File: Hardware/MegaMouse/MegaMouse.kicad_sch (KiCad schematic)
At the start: 0 parts

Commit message: Brake lights!
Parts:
- added BT101: Battery_Cell, Battery:BatteryHolder_MPD_BH-18650-PC2, symbol Device:Battery_Cell
- added D101, D102: BrakeLight, LED_THT:LED_D3.0mm_Horizontal_O1.27mm_Z2.0mm, symbol Device:LED
- added D103: TurnL, LED_THT:LED_D3.0mm_Horizontal_O6.35mm_Z6.0mm, symbol Device:LED
- added D104: TurnR, LED_THT:LED_D3.0mm_Horizontal_O6.35mm_Z6.0mm, symbol Device:LED
- added J101: MotorL, MegaMouse:MicroMotor, symbol Connector:Conn_01x05_Female
- added J102: MotorR, MegaMouse:MicroMotor, symbol Connector:Conn_01x05_Female
- added U101: ATmega328P-A, Package_QFP:TQFP-32_7x7mm_P0.8mm, symbol MCU_Microchip_ATmega:ATmega328P-A
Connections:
- new net: U101.21 (GND), U101.3 (GND), U101.5 (GND)
- new net: U101.4 (VCC), U101.6 (VCC)
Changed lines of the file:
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@@
 (kicad_sch (version 20211123) (generator eeschema)
   (paper "A4")
+  (symbol (lib_id "Device:LED") (at 71.755 76.835 180) (unit 1)
+    (in_bom yes) (on_board yes) (fields_autoplaced)
+    (property "Reference" "D101" (id 0) (at 73.3425 69.85 0))
+    (property "Value" "BrakeLight" (id 1) (at 73.3425 72.39 0))
+    (property "Footprint" "LED_THT:LED_D3.0mm_Horizontal_O1.27mm_Z2.0mm" (id 2) (at 71.755 76.835 0)
+      (effects (font (size 1.27 1.27)) hide)
+    )
+    (property "Datasheet" "~" (id 3) (at 71.755 76.835 0)
+      (effects (font (size 1.27 1.27)) hide)
+    )
+    (pin "1")
+    (pin "2")
+  )
+  (symbol (lib_id "Device:Battery_Cell") (at 234.95 49.53 0) (unit 1)
+    (in_bom yes) (on_board yes) (fields_autoplaced)
+    (property "Reference" "BT101" (id 0) (at 238.76 46.2279 0)
+      (effects (font (size 1.27 1.27)) (justify left))
+    )
+    (property "Value" "Battery_Cell" (id 1) (at 238.76 48.7679 0)
+      (effects (font (size 1.27 1.27)) (justify left))
+    )
+    (property "Footprint" "Battery:BatteryHolder_MPD_BH-18650-PC2" (id 2) (at 234.95 48.006 90)
+      (effects (font (size 1.27 1.27)) hide)
+    )
+    (property "Datasheet" "~" (id 3) (at 234.95 48.006 90)
+      (effects (font (size 1.27 1.27)) hide)
+    )
+    (pin "1")
+    (pin "2")
+  )
+  (symbol (lib_id "MCU_Microchip_ATmega:ATmega328P-A") (at 142.24 96.52 0) (unit 1)
+    (in_bom yes) (on_board yes) (fields_autoplaced)
+    (property "Reference" "U101" (id 0) (at 144.2594 134.62 0)
+      (effects (font (size 1.27 1.27)) (justify left))
+    )
+    (property "Value" "ATmega328P-A" (id 1) (at 144.2594 137.16 0)
+      (effects (font (size 1.27 1.27)) (justify left))
+    )
+    (property "Footprint" "Package_QFP:TQFP-32_7x7mm_P0.8mm" (id 2) (at 142.24 96.52 0)
+      (effects (font (size 1.27 1.27) italic) hide)
+    )
+    (property "Datasheet" "http://ww1.microchip.com/downloads/en/DeviceDoc/ATmega328_P%20AVR%20MCU%20with%20picoPower%20Technology%20Data%20Sheet%2040001984A.pdf" (id 3) (at 142.24 96.52 0)
+      (effects (font (size 1.27 1.27)) hide)
+    )
+    (pin "1")
+    (pin "10")
+    (pin "11")
+    (pin "12")
+    (pin "13")
+    (pin "14")
+    (pin "15")
+    (pin "16")
+    (pin "17")
+    (pin "18")
+    (pin "19")
+    (pin "2")
+    (pin "20")
+    (pin "21")
+    (pin "22")
+    (pin "23")
+    (pin "24")
+    (pin "25")
+    (pin "26")
+    (pin "27")
+    (pin "28")
+    (pin "29")
+    (pin "3")
+    (pin "30")
+    (pin "31")
+    (pin "32")
+    (pin "4")
+    (pin "5")
+    (pin "6")
+    (pin "7")
+    (pin "8")
+    (pin "9")
+  )
+  (symbol (lib_id "Device:LED") (at 85.09 76.835 180) (unit 1)
+    (in_bom yes) (on_board yes) (fields_autoplaced)
+    (property "Reference" "D103" (id 0) (at 86.6775 69.215 0))
+    (property "Value" "TurnL" (id 1) (at 86.6775 71.755 0))
+    (property "Footprint" "LED_THT:LED_D3.0mm_Horizontal_O6.35mm_Z6.0mm" (id 2) (at 85.09 76.835 0)
+      (effects (font (size 1.27 1.27)) hide)
+    )
+    (property "Datasheet" "~" (id 3) (at 85.09 76.835 0)
+      (effects (font (size 1.27 1.27)) hide)
+    )
+    (pin "1")
+    (pin "2")
+  )
+  (symbol (lib_id "Device:LED") (at 85.09 87.63 180) (unit 1)
+    (in_bom yes) (on_board yes) (fields_autoplaced)
+    (property "Reference" "D104" (id 0) (at 86.6775 80.01 0))
+    (property "Value" "TurnR" (id 1) (at 86.6775 82.55 0))
+    (property "Footprint" "LED_THT:LED_D3.0mm_Horizontal_O6.35mm_Z6.0mm" (id 2) (at 85.09 87.63 0)
+      (effects (font (size 1.27 1.27)) hide)
+    )
+    (property "Datasheet" "~" (id 3) (at 85.09 87.63 0)
+      (effects (font (size 1.27 1.27)) hide)
+    )
+    (pin "1")
+    (pin "2")
+  )
+  (symbol (lib_id "Device:LED") (at 71.755 87.63 180) (unit 1)
+    (in_bom yes) (on_board yes) (fields_autoplaced)
+    (property "Reference" "D102" (id 0) (at 73.3425 80.645 0))
+    (property "Value" "BrakeLight" (id 1) (at 73.3425 83.185 0))
+    (property "Footprint" "LED_THT:LED_D3.0mm_Horizontal_O1.27mm_Z2.0mm" (id 2) (at 71.755 87.63 0)
+      (effects (font (size 1.27 1.27)) hide)
+    )
+    (property "Datasheet" "~" (id 3) (at 71.755 87.63 0)
+      (effects (font (size 1.27 1.27)) hide)
+    )
+    (pin "1")
+    (pin "2")
+  )
+  (symbol (lib_id "Connector:Conn_01x05_Female") (at 205.74 85.725 0) (unit 1)
+    (in_bom yes) (on_board yes) (fields_autoplaced)
+    (property "Reference" "J101" (id 0) (at 207.01 84.4549 0)
+      (effects (font (size 1.27 1.27)) (justify left))
+    )
+    (property "Value" "MotorL" (id 1) (at 207.01 86.9949 0)
+      (effects (font (size 1.27 1.27)) (justify left))
+    )
+    (property "Footprint" "MegaMouse:MicroMotor" (id 2) (at 205.74 85.725 0)
+      (effects (font (size 1.27 1.27)) hide)
+    )
+    (property "Datasheet" "~" (id 3) (at 205.74 85.725 0)
+      (effects (font (size 1.27 1.27)) hide)
+    )
+    (pin "1")
+    (pin "2")
+    (pin "3")
+    (pin "4")
+    (pin "5")
+  )
+  (symbol (lib_id "Connector:Conn_01x05_Female") (at 222.25 85.725 0) (unit 1)
+    (in_bom yes) (on_board yes) (fields_autoplaced)
+    (property "Reference" "J102" (id 0) (at 223.52 84.4549 0)
+      (effects (font (size 1.27 1.27)) (justify left))
+    )
+    (property "Value" "MotorR" (id 1) (at 223.52 86.9949 0)
+      (effects (font (size 1.27 1.27)) (justify left))
+    )
+    (property "Footprint" "MegaMouse:MicroMotor" (id 2) (at 222.25 85.725 0)
+      (effects (font (size 1.27 1.27)) hide)
+    )
+    (property "Datasheet" "~" (id 3) (at 222.25 85.725 0)
+      (effects (font (size 1.27 1.27)) hide)
+    )
+    (pin "1")
+    (pin "2")
+    (pin "3")
+    (pin "4")
+    (pin "5")
+  )
   (sheet_instances
     (path "/" (page "1"))
   )
+  (symbol_instances
+    (path "/3108476a-847a-4adf-becb-69126938c9dd"
+      (reference "BT101") (unit 1) (value "Battery_Cell") (footprint "Battery:BatteryHolder_MPD_BH-18650-PC2")
+    )
+    (path "/0b0f8615-a521-40dd-95b3-c6dc98e26914"
+      (reference "D101") (unit 1) (value "BrakeLight") (footprint "LED_THT:LED_D3.0mm_Horizontal_O1.27mm_Z2.0mm")
+    )
+    (path "/b6bd84fa-c83d-44d0-90d2-a9564b93df9c"
+      (reference "D102") (unit 1) (value "BrakeLight") (footprint "LED_THT:LED_D3.0mm_Horizontal_O1.27mm_Z2.0mm")
+    )
+    (path "/87589939-cb7a-482a-9d88-508640d671a3"
+      (reference "D103") (unit 1) (value "TurnL") (footprint "LED_THT:LED_D3.0mm_Horizontal_O6.35mm_Z6.0mm")
+    )
+    (path "/b06c9f42-4c7e-4451-b623-83e43d24c5fc"
+      (reference "D104") (unit 1) (value "TurnR") (footprint "LED_THT:LED_D3.0mm_Horizontal_O6.35mm_Z6.0mm")
+    )
+    (path "/bd1226fe-f6ac-4ec8-9650-08c99a4f03a9"
+      (reference "J101") (unit 1) (value "MotorL") (footprint "MegaMouse:MicroMotor")
+    )
+    (path "/e73cdaaa-7743-4e85-b32f-0823784545c7"
+      (reference "J102") (unit 1) (value "MotorR") (footprint "MegaMouse:MicroMotor")
+    )
+    (path "/6237422b-5d80-4047-94aa-94384be9ec54"
+      (reference "U101") (unit 1) (value "ATmega328P-A") (footprint "Package_QFP:TQFP-32_7x7mm_P0.8mm")
+    )
+  )
 )

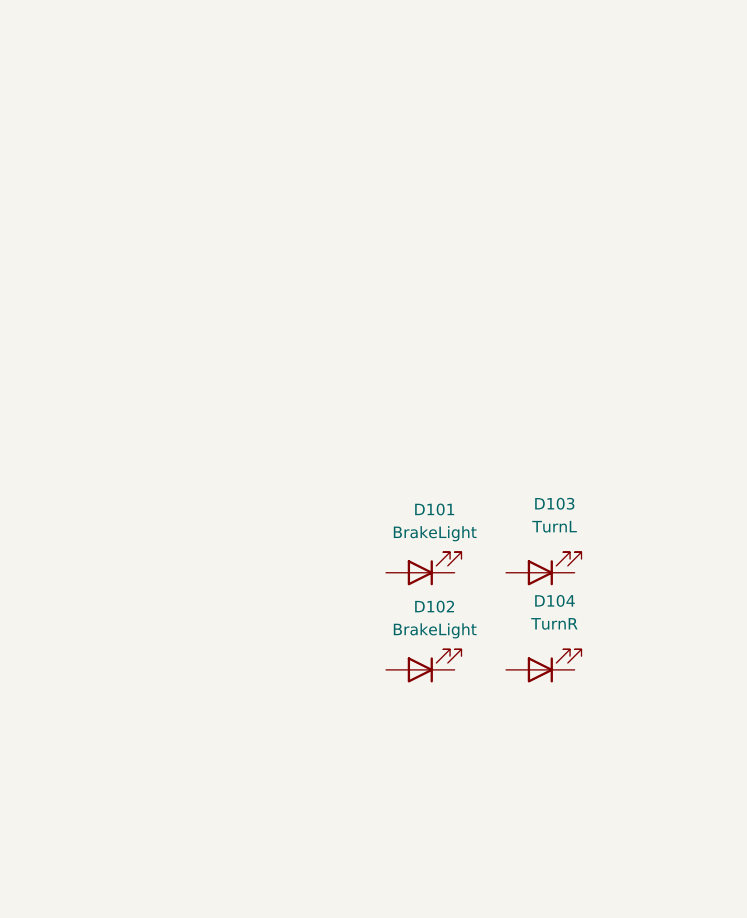
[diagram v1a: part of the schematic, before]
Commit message: Add brakelight as full kicad_mod
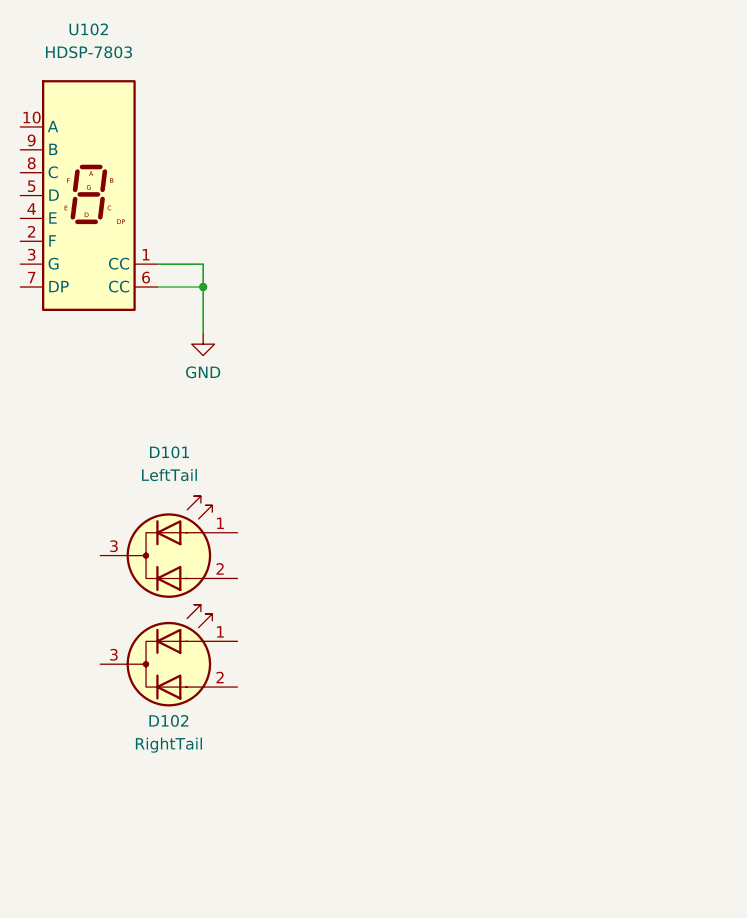
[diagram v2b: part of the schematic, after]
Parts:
- removed D101, D102: BrakeLight, LED_THT:LED_D3.0mm_Horizontal_O1.27mm_Z2.0mm, symbol Device:LED
- removed D103: TurnL, LED_THT:LED_D3.0mm_Horizontal_O6.35mm_Z6.0mm, symbol Device:LED
- removed D104: TurnR, LED_THT:LED_D3.0mm_Horizontal_O6.35mm_Z6.0mm, symbol Device:LED
- added D101: LeftTail, MegaMouse:BrakeLight, symbol Device:LED_Dual_AAK
- added D102: RightTail, MegaMouse:BrakeLight, symbol Device:LED_Dual_AAK
- added U102: HDSP-7803, Display_7Segment:HDSP-7801, symbol Display_Character:HDSP-7803
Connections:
- new net GND: U102.1 (CC), U102.6 (CC)
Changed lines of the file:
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@@
 (kicad_sch (version 20211123) (generator eeschema)
   (paper "A4")
-  (symbol (lib_id "Device:LED") (at 71.755 76.835 180) (unit 1)
-    (in_bom yes) (on_board yes) (fields_autoplaced)
-    (property "Reference" "D101" (id 0) (at 73.3425 69.85 0))
-    (property "Value" "BrakeLight" (id 1) (at 73.3425 72.39 0))
-    (property "Footprint" "LED_THT:LED_D3.0mm_Horizontal_O1.27mm_Z2.0mm" (id 2) (at 71.755 76.835 0)
-      (effects (font (size 1.27 1.27)) hide)
-    )
-    (property "Datasheet" "~" (id 3) (at 71.755 76.835 0)
-      (effects (font (size 1.27 1.27)) hide)
-    )
-    (pin "1")
-    (pin "2")
+  (junction (at 47.625 45.085) (diameter 0) (color 0 0 0 0)
+  )
+  (wire (pts (xy 47.625 42.545) (xy 47.625 45.085))
+    (stroke (width 0) (type default) (color 0 0 0 0))
+  )
+  (wire (pts (xy 42.545 42.545) (xy 47.625 42.545))
+    (stroke (width 0) (type default) (color 0 0 0 0))
+  )
+  (wire (pts (xy 47.625 45.085) (xy 47.625 50.165))
+    (stroke (width 0) (type default) (color 0 0 0 0))
+  )
+  (wire (pts (xy 42.545 45.085) (xy 47.625 45.085))
+    (stroke (width 0) (type default) (color 0 0 0 0))
+  )
+  (symbol (lib_id "Display_Character:HDSP-7803") (at 34.925 34.925 0) (unit 1)
+    (in_bom yes) (on_board yes) (fields_autoplaced)
+    (property "Reference" "U102" (id 0) (at 34.925 16.51 0))
+    (property "Value" "HDSP-7803" (id 1) (at 34.925 19.05 0))
+    (property "Footprint" "Display_7Segment:HDSP-7801" (id 2) (at 34.925 48.895 0)
+      (effects (font (size 1.27 1.27)) hide)
+    )
+    (property "Datasheet" "https://docs.broadcom.com/docs/AV02-2553EN" (id 3) (at 34.925 34.925 0)
+      (effects (font (size 1.27 1.27)) hide)
+    )
+    (pin "1")
+    (pin "10")
+    (pin "2")
+    (pin "3")
+    (pin "4")
+    (pin "5")
+    (pin "6")
+    (pin "7")
+    (pin "8")
+    (pin "9")
   )
   (symbol (lib_id "Device:Battery_Cell") (at 234.95 49.53 0) (unit 1)
@@
     (pin "9")
   )
-  (symbol (lib_id "Device:LED") (at 85.09 76.835 180) (unit 1)
-    (in_bom yes) (on_board yes) (fields_autoplaced)
-    (property "Reference" "D103" (id 0) (at 86.6775 69.215 0))
-    (property "Value" "TurnL" (id 1) (at 86.6775 71.755 0))
-    (property "Footprint" "LED_THT:LED_D3.0mm_Horizontal_O6.35mm_Z6.0mm" (id 2) (at 85.09 76.835 0)
-      (effects (font (size 1.27 1.27)) hide)
-    )
-    (property "Datasheet" "~" (id 3) (at 85.09 76.835 0)
-      (effects (font (size 1.27 1.27)) hide)
-    )
-    (pin "1")
-    (pin "2")
-  )
-  (symbol (lib_id "Device:LED") (at 85.09 87.63 180) (unit 1)
-    (in_bom yes) (on_board yes) (fields_autoplaced)
-    (property "Reference" "D104" (id 0) (at 86.6775 80.01 0))
-    (property "Value" "TurnR" (id 1) (at 86.6775 82.55 0))
-    (property "Footprint" "LED_THT:LED_D3.0mm_Horizontal_O6.35mm_Z6.0mm" (id 2) (at 85.09 87.63 0)
-      (effects (font (size 1.27 1.27)) hide)
-    )
-    (property "Datasheet" "~" (id 3) (at 85.09 87.63 0)
-      (effects (font (size 1.27 1.27)) hide)
-    )
-    (pin "1")
-    (pin "2")
-  )
-  (symbol (lib_id "Device:LED") (at 71.755 87.63 180) (unit 1)
-    (in_bom yes) (on_board yes) (fields_autoplaced)
-    (property "Reference" "D102" (id 0) (at 73.3425 80.645 0))
-    (property "Value" "BrakeLight" (id 1) (at 73.3425 83.185 0))
-    (property "Footprint" "LED_THT:LED_D3.0mm_Horizontal_O1.27mm_Z2.0mm" (id 2) (at 71.755 87.63 0)
-      (effects (font (size 1.27 1.27)) hide)
-    )
-    (property "Datasheet" "~" (id 3) (at 71.755 87.63 0)
-      (effects (font (size 1.27 1.27)) hide)
-    )
-    (pin "1")
-    (pin "2")
+  (symbol (lib_id "power:GND") (at 47.625 50.165 0) (unit 1)
+    (in_bom yes) (on_board yes) (fields_autoplaced)
+    (property "Reference" "#PWR0101" (id 0) (at 47.625 56.515 0)
+      (effects (font (size 1.27 1.27)) hide)
+    )
+    (property "Value" "GND" (id 1) (at 47.625 54.61 0))
+    (property "Footprint" "" (id 2) (at 47.625 50.165 0)
+      (effects (font (size 1.27 1.27)) hide)
+    )
+    (property "Datasheet" "" (id 3) (at 47.625 50.165 0)
+      (effects (font (size 1.27 1.27)) hide)
+    )
+    (pin "1")
+  )
+  (symbol (lib_id "Device:LED_Dual_AAK") (at 43.815 86.995 0) (unit 1)
+    (in_bom yes) (on_board yes)
+    (property "Reference" "D102" (id 0) (at 43.815 93.345 0))
+    (property "Value" "RightTail" (id 1) (at 43.815 95.885 0))
+    (property "Footprint" "MegaMouse:BrakeLight" (id 2) (at 43.815 86.995 0)
+      (effects (font (size 1.27 1.27)) hide)
+    )
+    (property "Datasheet" "~" (id 3) (at 43.815 86.995 0)
+      (effects (font (size 1.27 1.27)) hide)
+    )
+    (pin "1")
+    (pin "2")
+    (pin "3")
   )
   (symbol (lib_id "Connector:Conn_01x05_Female") (at 205.74 85.725 0) (unit 1)
@@
     (pin "4")
     (pin "5")
+  )
+  (symbol (lib_id "Device:LED_Dual_AAK") (at 43.815 74.93 0) (unit 1)
+    (in_bom yes) (on_board yes) (fields_autoplaced)
+    (property "Reference" "D101" (id 0) (at 43.8785 63.5 0))
+    (property "Value" "LeftTail" (id 1) (at 43.8785 66.04 0))
+    (property "Footprint" "MegaMouse:BrakeLight" (id 2) (at 43.815 74.93 0)
+      (effects (font (size 1.27 1.27)) hide)
+    )
+    (property "Datasheet" "~" (id 3) (at 43.815 74.93 0)
+      (effects (font (size 1.27 1.27)) hide)
+    )
+    (pin "1")
+    (pin "2")
+    (pin "3")
   )
   (symbol (lib_id "Connector:Conn_01x05_Female") (at 222.25 85.725 0) (unit 1)
@@
   )
   (symbol_instances
+    (path "/680546ea-6597-4380-9e70-360320128715"
+      (reference "#PWR0101") (unit 1) (value "GND") (footprint "")
+    )
     (path "/3108476a-847a-4adf-becb-69126938c9dd"
       (reference "BT101") (unit 1) (value "Battery_Cell") (footprint "Battery:BatteryHolder_MPD_BH-18650-PC2")
     )
-    (path "/0b0f8615-a521-40dd-95b3-c6dc98e26914"
-      (reference "D101") (unit 1) (value "BrakeLight") (footprint "LED_THT:LED_D3.0mm_Horizontal_O1.27mm_Z2.0mm")
-    )
-    (path "/b6bd84fa-c83d-44d0-90d2-a9564b93df9c"
-      (reference "D102") (unit 1) (value "BrakeLight") (footprint "LED_THT:LED_D3.0mm_Horizontal_O1.27mm_Z2.0mm")
-    )
-    (path "/87589939-cb7a-482a-9d88-508640d671a3"
-      (reference "D103") (unit 1) (value "TurnL") (footprint "LED_THT:LED_D3.0mm_Horizontal_O6.35mm_Z6.0mm")
-    )
-    (path "/b06c9f42-4c7e-4451-b623-83e43d24c5fc"
-      (reference "D104") (unit 1) (value "TurnR") (footprint "LED_THT:LED_D3.0mm_Horizontal_O6.35mm_Z6.0mm")
+    (path "/ca9b22a2-b92f-47fd-a808-1f1f393a3eb7"
+      (reference "D101") (unit 1) (value "LeftTail") (footprint "MegaMouse:BrakeLight")
+    )
+    (path "/8ed1c7dc-a397-4ebb-878f-88bc55ae0384"
+      (reference "D102") (unit 1) (value "RightTail") (footprint "MegaMouse:BrakeLight")
     )
     (path "/bd1226fe-f6ac-4ec8-9650-08c99a4f03a9"
@@
       (reference "U101") (unit 1) (value "ATmega328P-A") (footprint "Package_QFP:TQFP-32_7x7mm_P0.8mm")
     )
-  )
+    (path "/07d9b08c-1968-419d-8cab-af1700401c87"
+      (reference "U102") (unit 1) (value "HDSP-7803") (footprint "Display_7Segment:HDSP-7801")
+    )
+  )
